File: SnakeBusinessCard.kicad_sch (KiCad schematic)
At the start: 0 parts

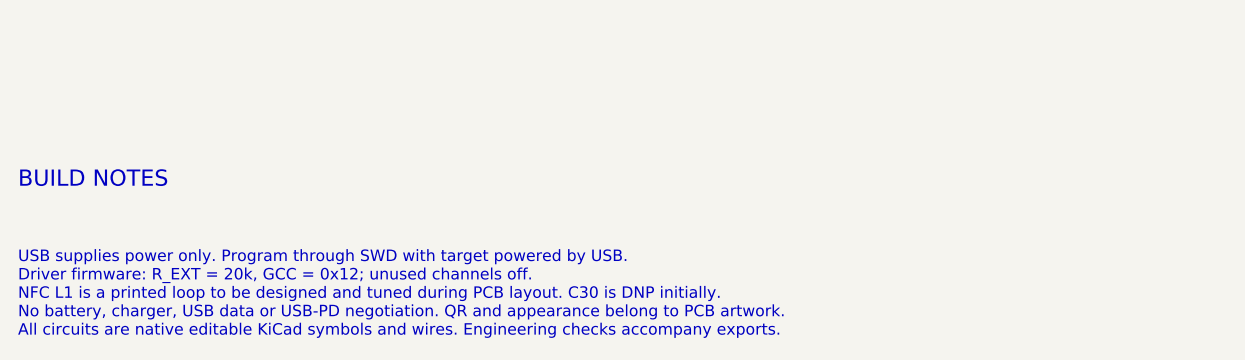
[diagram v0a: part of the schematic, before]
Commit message: Complete procurement BOM and document component review gates
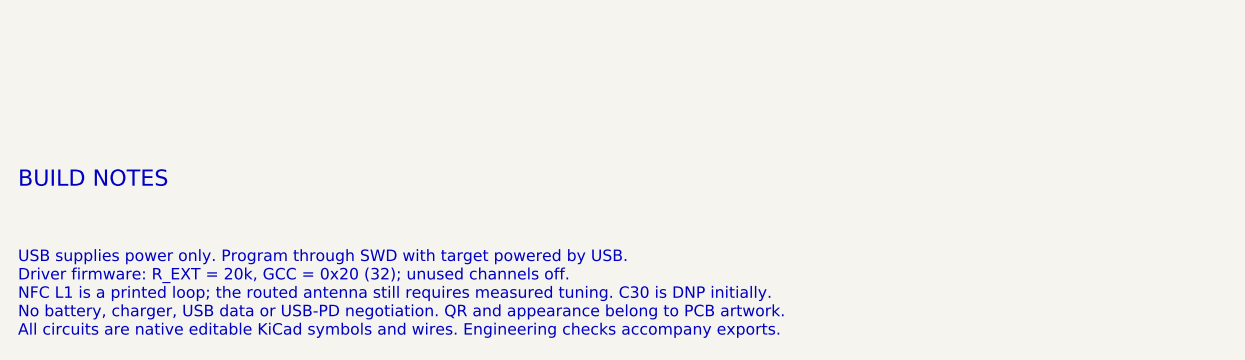
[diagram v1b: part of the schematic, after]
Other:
- note added: "USB supplies power only. Program through SWD with target powered by USB. Driver firmware: R_EXT = 20k, GCC = 0x20 (32); unused channels off. NFC L1 is a printed loop; the routed antenna still requires measured tuning. C30 is DNP initially. No battery, charger, USB data or USB-PD negotiation. QR and appearance belong to PCB artwork. All circuits are native editable KiCad symbols and wires. Enginee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"
- note removed: "USB supplies power only. Program through SWD with target powered by USB. Driver firmware: R_EXT = 20k, GCC = 0x12; unused channels off. NFC L1 is a printed loop to be designed and tuned during PCB layout. C30 is DNP initially. No battery, charger, USB data or USB-PD negotiation. QR and appearance belong to PCB artwork. All circuits are native editable KiCad symbols and wires. Engineering checks a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"
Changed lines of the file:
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@@
       (justify left))
 )
-  (text "USB supplies power only. Program through SWD with target powered by USB.\nDriver firmware: R_EXT = 20k, GCC = 0x12; unused channels off.\nNFC L1 is a printed loop to be designed and tuned during PCB layout. C30 is DNP initially.\nNo battery, charger, USB data or USB-PD negotiation. QR and appearance belong to PCB artwork.\nAll circuits are native editable KiCad symbols and wires. Engineering checks accompany exports."
+  (text "USB supplies power only. Program through SWD with target powered by USB.\nDriver firmware: R_EXT = 20k, GCC = 0x20 (32); unused channels off.\nNFC L1 is a printed loop; the routed antenna still requires measured tuning. C30 is DNP initially.\nNo battery, charger, USB data or USB-PD negotiation. QR and appearance belong to PCB artwork.\nAll circuits are native editable KiCad symbols and wires. Engineering checks accompany exports."
     (at 20.32 218.44 0)
     (effects
